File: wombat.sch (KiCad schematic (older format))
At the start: 187 parts, among them J1 Conn_01x05, Q1 FDS6630A, SW1 SW_SPST, SW10 SW_SPST, SW101 SW_Push, SW11 SW_SPST, SW12 SW_SPST, SW13 SW_SPST, SW14 SW_SPST, SW15 SW_SPST, SW16 SW_SPST, SW17 SW_SPST, SW18 SW_SPST, SW19 SW_SPST, SW2 SW_SPST, SW20 SW_SPST, SW21 SW_SPST, SW22 SW_SPST, SW23 SW_SPST, SW24 SW_SPST, SW25 SW_SPST, SW26 SW_SPST, SW27 SW_SPST, SW28 SW_SPST, SW29 SW_SPST, SW3 SW_SPST, SW30 SW_SPST, SW31 SW_SPST, SW32 SW_SPST, SW33 SW_SPST, SW34 SW_SPST, SW35 SW_SPST, SW36 SW_SPST, SW37 SW_SPST, SW38 SW_SPST, SW39 SW_SPST, SW4 SW_SPST, SW40 SW_SPST, SW41 SW_SPST, SW42 SW_SPST, SW43 SW_SPST, SW44 SW_SPST, SW45 SW_SPST, SW46 SW_SPST, SW47 SW_SPST, SW48 SW_SPST, SW49 SW_SPST, SW5 SW_SPST, SW50 SW_SPST, SW51 SW_SPST, SW52 SW_SPST, SW6 SW_SPST, SW7 SW_SPST, SW8 SW_SPST, SW9 SW_SPST, U1 ProMicro

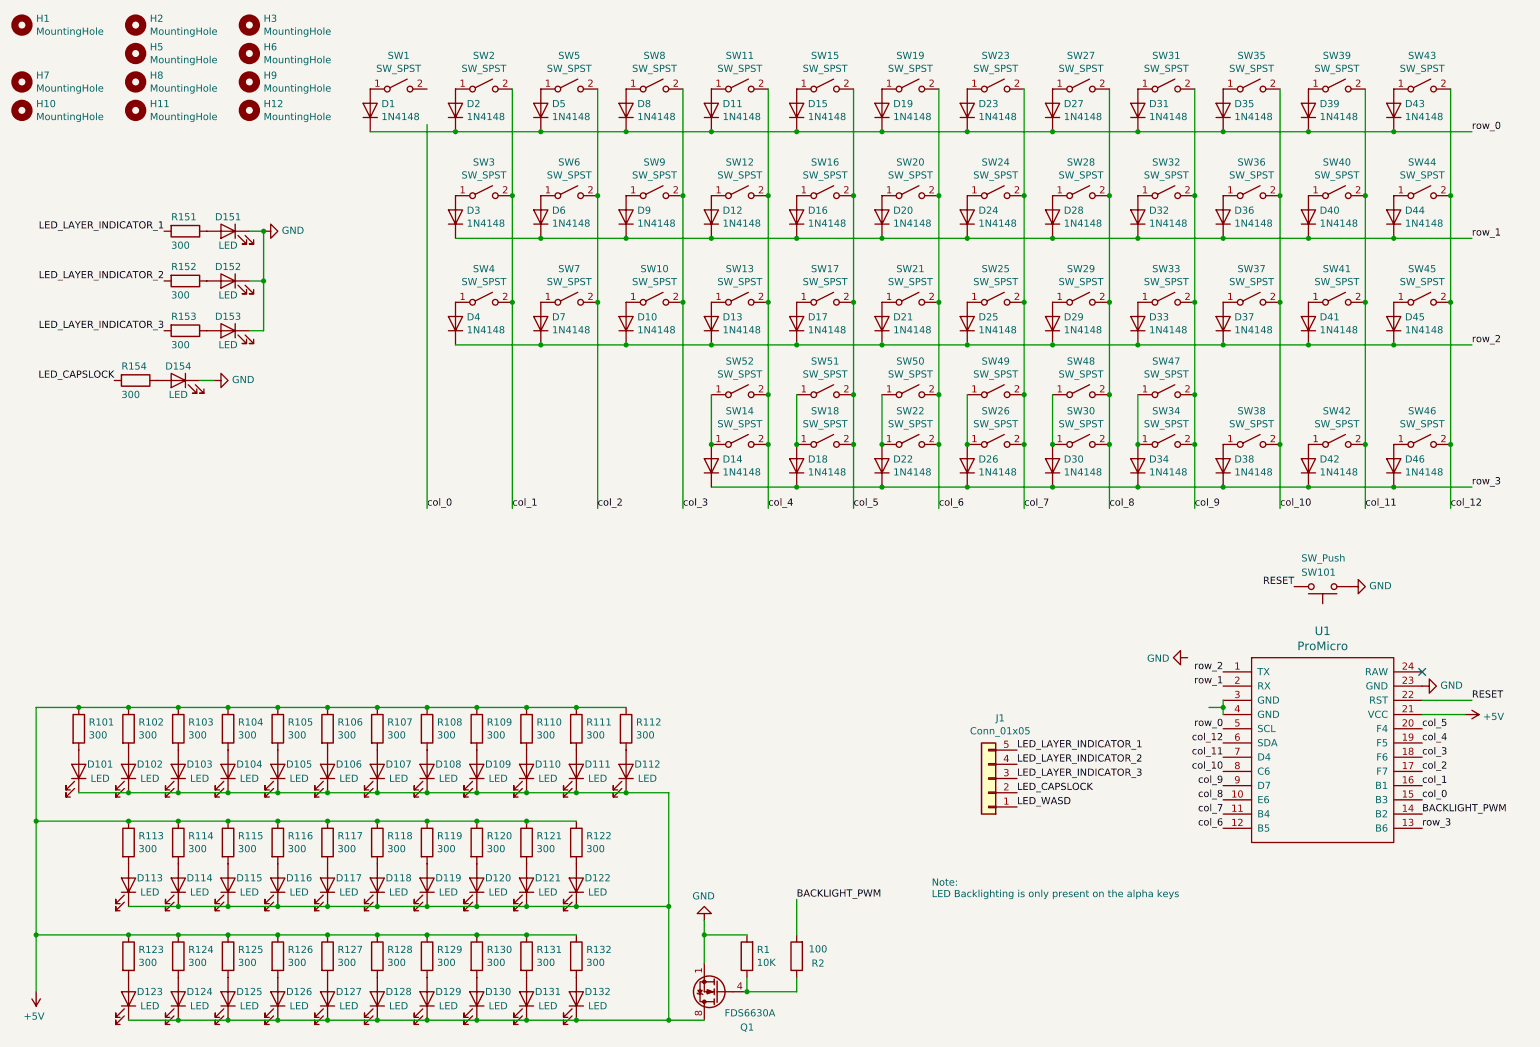
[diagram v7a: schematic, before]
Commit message: tidy up schematic. no changes no circuit
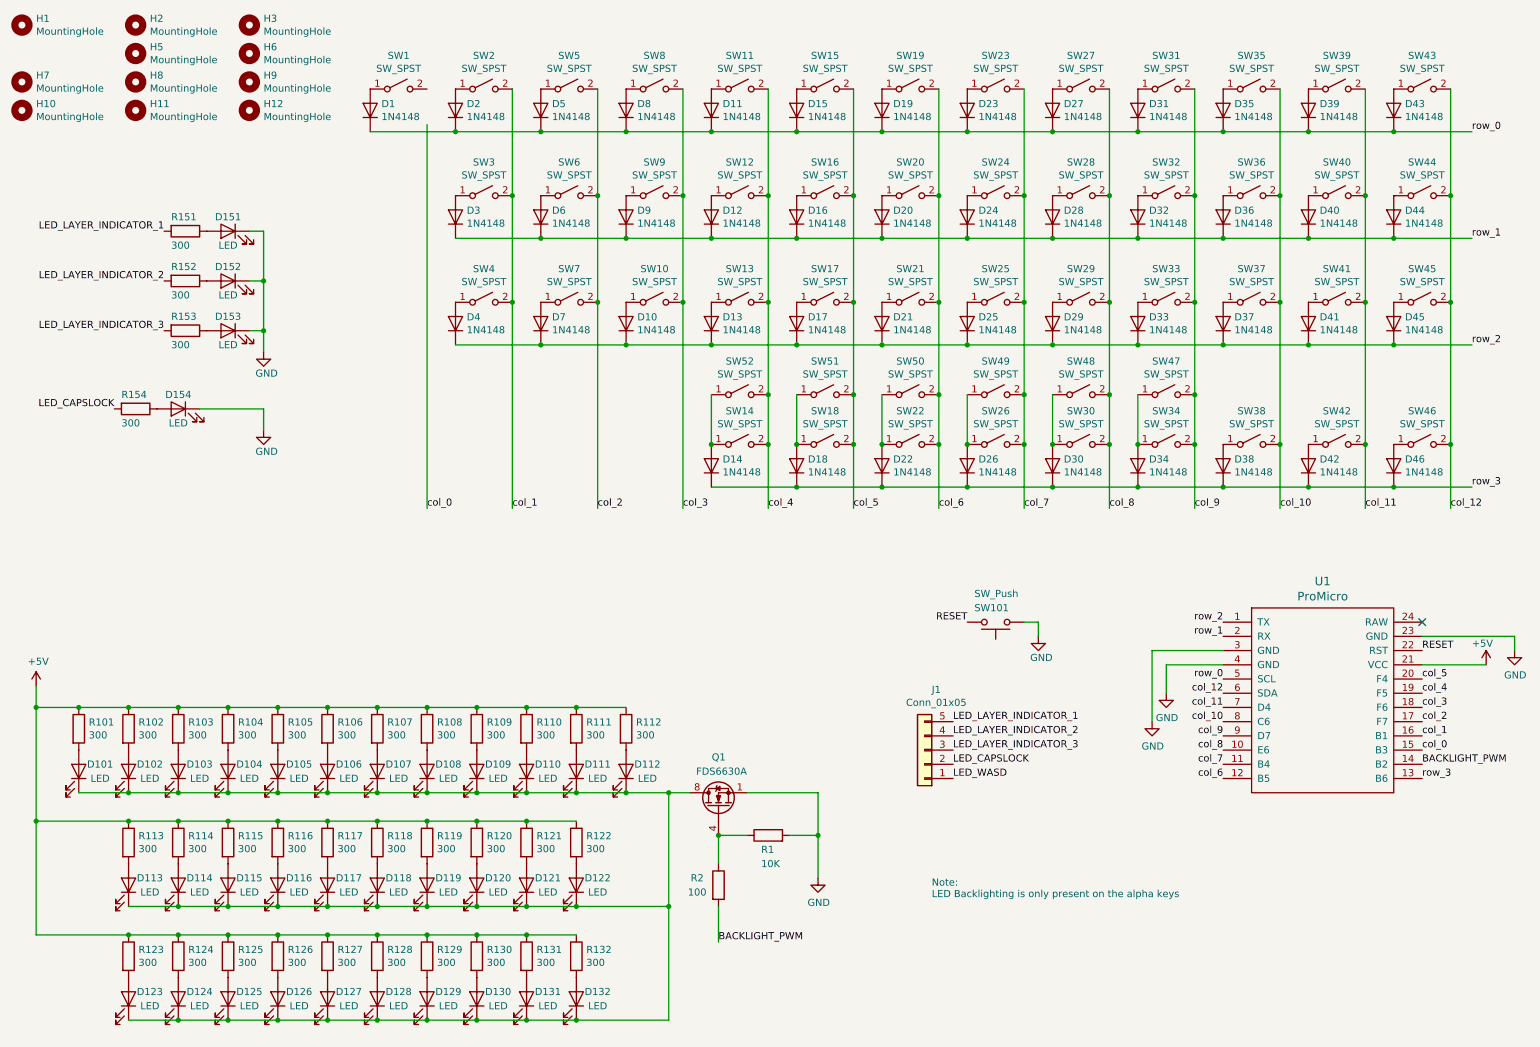
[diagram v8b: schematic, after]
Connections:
- net GND: now also U1.3 (GND), U1.4 (GND)
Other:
- moved on the sheet: D154, J1, Q1, R1, R154, R2, SW101, U1
